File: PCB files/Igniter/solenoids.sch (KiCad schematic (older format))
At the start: 15 parts, among them Q2 N MOSFET, Q3 N MOSFET, Q4 N MOSFET, Q5 N MOSFET, Q6 N MOSFET

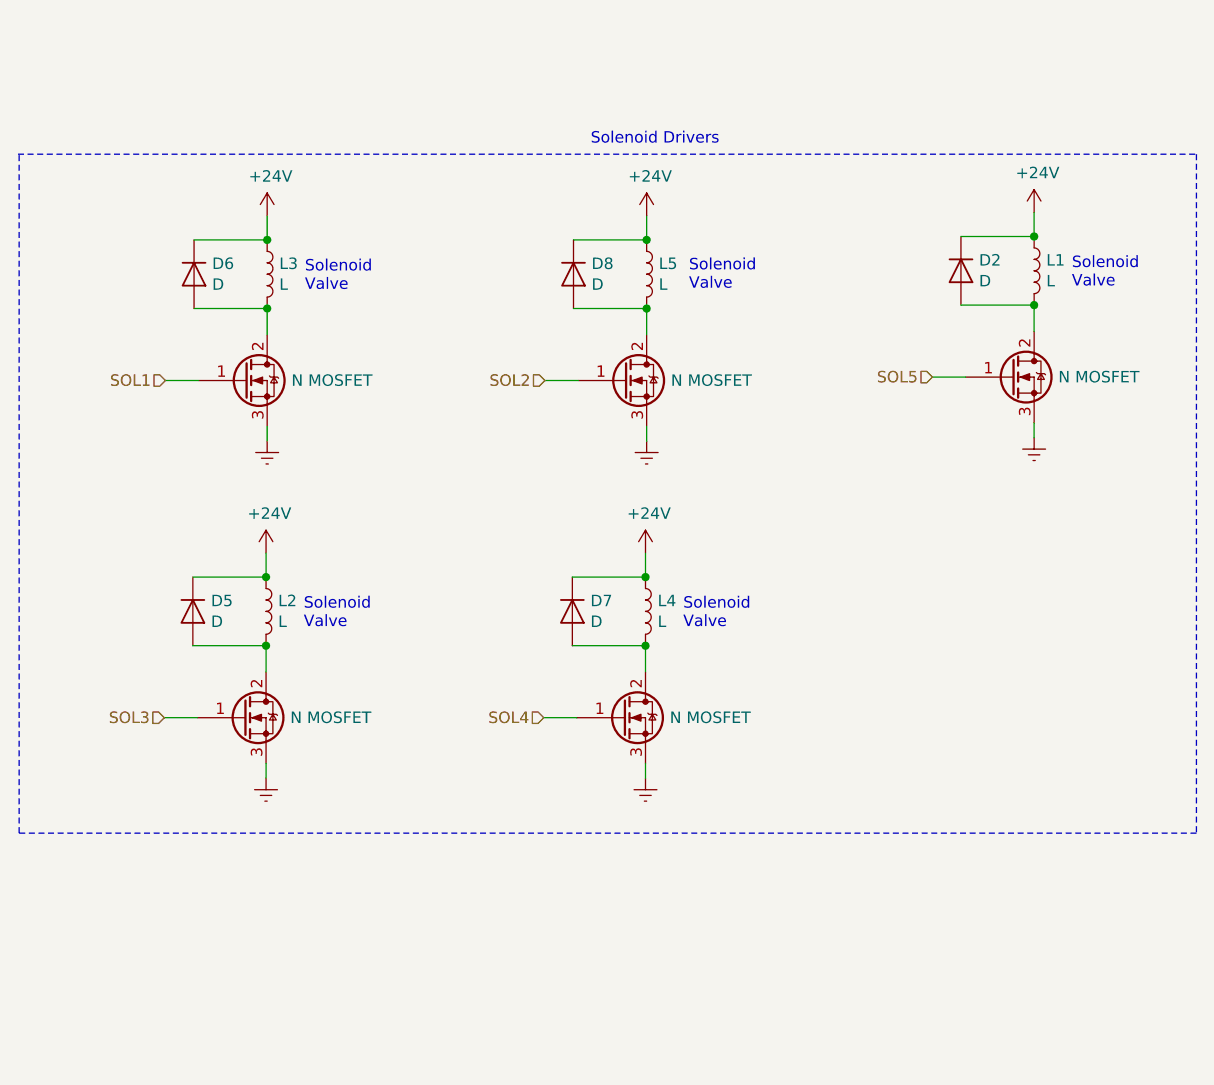
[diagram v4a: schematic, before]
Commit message: 11/1/2019
-Created bananajack footprint
-Began arranging components on board
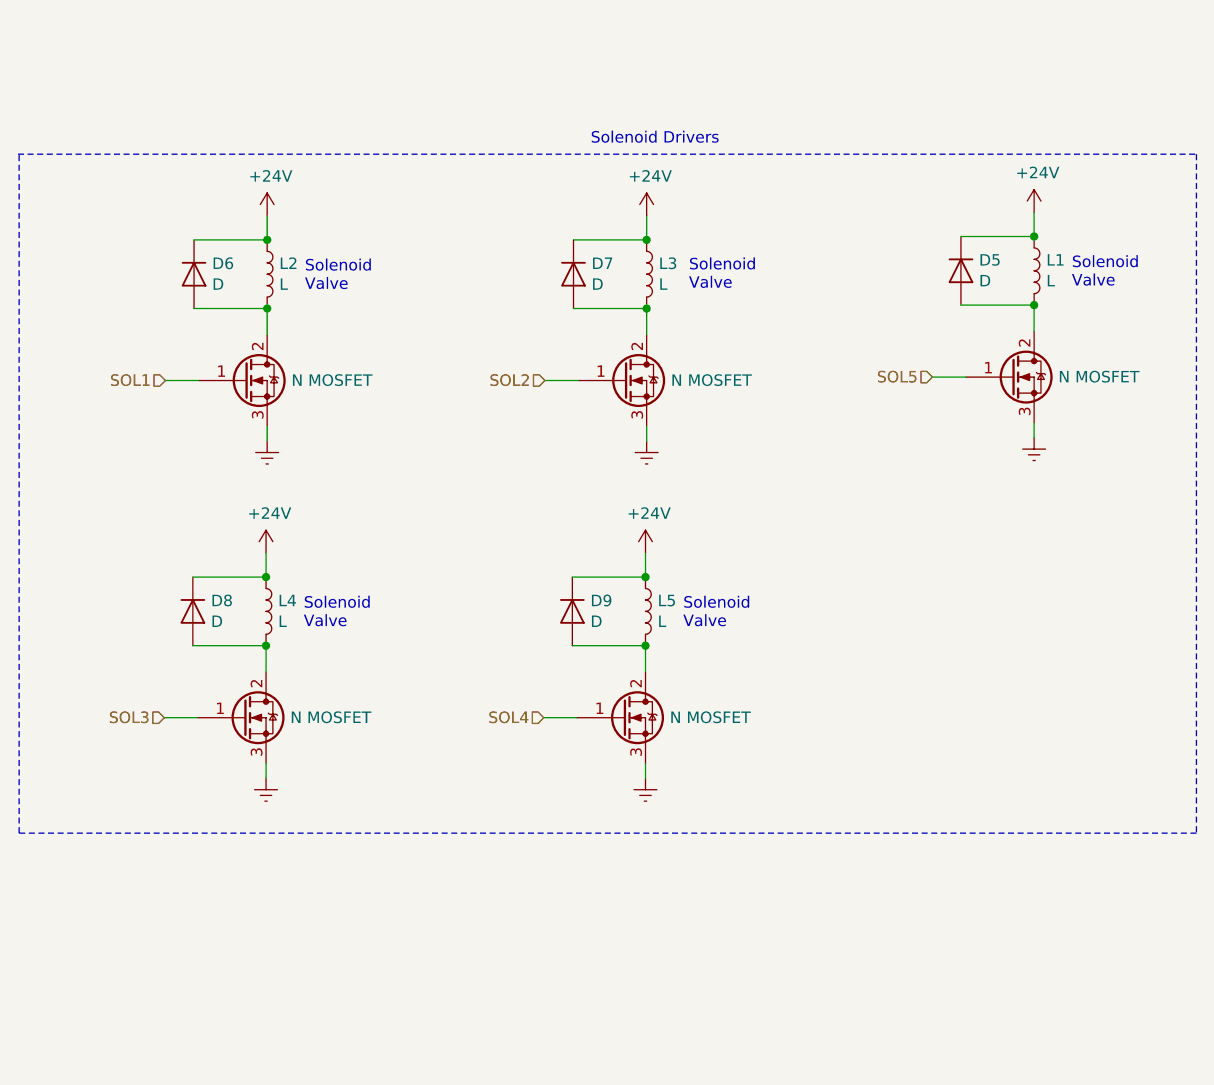
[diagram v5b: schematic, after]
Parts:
- renumbered D2 to D5, D8 to D7, D5 to D8, D7 to D9, L3 to L2, L5 to L3, L2 to L4, L4 to L5, Q4 to Q3, Q6 to Q4, Q3 to Q5, Q5 to Q6
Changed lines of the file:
@@
 LIBS:interface
 LIBS:Igniter-cache
-EELAYER 26 0
+EELAYER 29 0
 EELAYER END
 $Descr A4 11693 8268
@@
 Solenoid Drivers
 $Comp
-L Device:L L3
+L Device:L L2
 U 1 1 5DB4DF08
 P 4360 2815
-F 0 "L3" H 4413 2861 50  0000 L CNN
+F 0 "L2" H 4413 2861 50  0000 L CNN
 F 1 "L" H 4413 2770 50  0000 L CNN
 F 2 "" H 4360 2815 50  0001 C CNN
@@
 Connection ~ 4360 2965
 $Comp
-L power:GNDREF #PWR0108
+L power:GNDREF #PWR029
 U 1 1 5DB4DF2B
 P 4360 3545
-F 0 "#PWR0108" H 4360 3295 50  0001 C CNN
+F 0 "#PWR029" H 4360 3295 50  0001 C CNN
 F 1 "GNDREF" H 4365 3372 50  0001 C CNN
 F 2 "" H 4360 3545 50  0001 C CNN
@@
 	4360 3480 4360 3545
 $Comp
-L Device:L L2
+L Device:L L4
 U 1 1 5DB4DF33
 P 4355 4290
-F 0 "L2" H 4408 4336 50  0000 L CNN
+F 0 "L4" H 4408 4336 50  0000 L CNN
 F 1 "L" H 4408 4245 50  0000 L CNN
 F 2 "" H 4355 4290 50  0001 C CNN
@@
 $EndComp
 $Comp
-L Device:D D5
+L Device:D D8
 U 1 1 5DB4DF3A
 P 4035 4290
-F 0 "D5" V 3989 4369 50  0000 L CNN
+F 0 "D8" V 3989 4369 50  0000 L CNN
 F 1 "D" V 4080 4369 50  0000 L CNN
 F 2 "Diode_THT:D_DO-15_P12.70mm_Horizontal" H 4035 4290 50  0001 C CNN
@@
 Connection ~ 4355 4440
 $Comp
-L power:GNDREF #PWR0110
+L power:GNDREF #PWR033
 U 1 1 5DB4DF56
 P 4355 5020
-F 0 "#PWR0110" H 4355 4770 50  0001 C CNN
+F 0 "#PWR033" H 4355 4770 50  0001 C CNN
 F 1 "GNDREF" H 4360 4847 50  0001 C CNN
 F 2 "" H 4355 5020 50  0001 C CNN
@@
 	4355 4955 4355 5020
 $Comp
-L Device:L L5
+L Device:L L3
 U 1 1 5DB4DF5E
 P 6020 2815
-F 0 "L5" H 6073 2861 50  0000 L CNN
+F 0 "L3" H 6073 2861 50  0000 L CNN
 F 1 "L" H 6073 2770 50  0000 L CNN
 F 2 "" H 6020 2815 50  0001 C CNN
@@
 $EndComp
 $Comp
-L Device:D D8
+L Device:D D7
 U 1 1 5DB4DF65
 P 5700 2815
-F 0 "D8" V 5654 2894 50  0000 L CNN
+F 0 "D7" V 5654 2894 50  0000 L CNN
 F 1 "D" V 5745 2894 50  0000 L CNN
 F 2 "Diode_THT:D_DO-15_P12.70mm_Horizontal" H 5700 2815 50  0001 C CNN
@@
 Connection ~ 6020 2965
 $Comp
-L power:GNDREF #PWR0112
+L power:GNDREF #PWR030
 U 1 1 5DB4DF80
 P 6020 3545
-F 0 "#PWR0112" H 6020 3295 50  0001 C CNN
+F 0 "#PWR030" H 6020 3295 50  0001 C CNN
 F 1 "GNDREF" H 6025 3372 50  0001 C CNN
 F 2 "" H 6020 3545 50  0001 C CNN
@@
 	6020 3480 6020 3545
 $Comp
-L Device:L L4
+L Device:L L5
 U 1 1 5DB4DF88
 P 6015 4290
-F 0 "L4" H 6068 4336 50  0000 L CNN
+F 0 "L5" H 6068 4336 50  0000 L CNN
 F 1 "L" H 6068 4245 50  0000 L CNN
 F 2 "" H 6015 4290 50  0001 C CNN
@@
 $EndComp
 $Comp
-L Device:D D7
+L Device:D D9
 U 1 1 5DB4DF8F
 P 5695 4290
-F 0 "D7" V 5649 4369 50  0000 L CNN
+F 0 "D9" V 5649 4369 50  0000 L CNN
 F 1 "D" V 5740 4369 50  0000 L CNN
 F 2 "Diode_THT:D_DO-15_P12.70mm_Horizontal" H 5695 4290 50  0001 C CNN
@@
 Connection ~ 6015 4440
 $Comp
-L power:GNDREF #PWR0114
+L power:GNDREF #PWR034
 U 1 1 5DB4DFAB
 P 6015 5020
-F 0 "#PWR0114" H 6015 4770 50  0001 C CNN
+F 0 "#PWR034" H 6015 4770 50  0001 C CNN
 F 1 "GNDREF" H 6020 4847 50  0001 C CNN
 F 2 "" H 6015 5020 50  0001 C CNN
@@
 AR Path="/5D9BEB88/5DB4DFB4" Ref="Q?"  Part="1"
 AR Path="/5DB4DFB4" Ref="Q?"  Part="1"
-AR Path="/5DB4D508/5DB4DFB4" Ref="Q4"  Part="1"
-F 0 "Q4" H 4466 3326 50  0001 L CNN
+AR Path="/5DB4D508/5DB4DFB4" Ref="Q3"  Part="1"
+F 0 "Q3" H 4466 3326 50  0001 L CNN
 F 1 "N MOSFET" H 4466 3280 50  0000 L CNN
 F 2 "Package_TO_SOT_THT:TO-220-3_Horizontal_TabDown" H 4460 3380 50  0001 C CNN
@@
 AR Path="/5D9BEB88/5DB4DFBA" Ref="Q?"  Part="1"
 AR Path="/5DB4DFBA" Ref="Q?"  Part="1"
-AR Path="/5DB4D508/5DB4DFBA" Ref="Q6"  Part="1"
-F 0 "Q6" H 6126 3326 50  0001 L CNN
+AR Path="/5DB4D508/5DB4DFBA" Ref="Q4"  Part="1"
+F 0 "Q4" H 6126 3326 50  0001 L CNN
 F 1 "N MOSFET" H 6126 3280 50  0000 L CNN
 F 2 "Package_TO_SOT_THT:TO-220-3_Horizontal_TabDown" H 6120 3380 50  0001 C CNN
@@
 AR Path="/5D9BEB88/5DB4DFC0" Ref="Q?"  Part="1"
 AR Path="/5DB4DFC0" Ref="Q?"  Part="1"
-AR Path="/5DB4D508/5DB4DFC0" Ref="Q5"  Part="1"
-F 0 "Q5" H 6121 4801 50  0001 L CNN
+AR Path="/5DB4D508/5DB4DFC0" Ref="Q6"  Part="1"
+F 0 "Q6" H 6121 4801 50  0001 L CNN
 F 1 "N MOSFET" H 6121 4755 50  0000 L CNN
 F 2 "Package_TO_SOT_THT:TO-220-3_Horizontal_TabDown" H 6115 4855 50  0001 C CNN
@@
 AR Path="/5D9BEB88/5DB4DFC6" Ref="Q?"  Part="1"
 AR Path="/5DB4DFC6" Ref="Q?"  Part="1"
-AR Path="/5DB4D508/5DB4DFC6" Ref="Q3"  Part="1"
-F 0 "Q3" H 4461 4801 50  0001 L CNN
+AR Path="/5DB4D508/5DB4DFC6" Ref="Q5"  Part="1"
+F 0 "Q5" H 4461 4801 50  0001 L CNN
 F 1 "N MOSFET" H 4461 4755 50  0000 L CNN
 F 2 "Package_TO_SOT_THT:TO-220-3_Horizontal_TabDown" H 4455 4855 50  0001 C CNN
@@
 $EndComp
 $Comp
-L Device:D D2
+L Device:D D5
 U 1 1 5DB4DFD3
 P 7395 2800
-F 0 "D2" V 7349 2879 50  0000 L CNN
+F 0 "D5" V 7349 2879 50  0000 L CNN
 F 1 "D" V 7440 2879 50  0000 L CNN
 F 2 "Diode_THT:D_DO-15_P10.16mm_Horizontal" H 7395 2800 50  0001 C CNN
@@
 Connection ~ 7715 2950
 $Comp
-L power:GNDREF #PWR0116
+L power:GNDREF #PWR028
 U 1 1 5DB4DFEF
 P 7715 3530
-F 0 "#PWR0116" H 7715 3280 50  0001 C CNN
+F 0 "#PWR028" H 7715 3280 50  0001 C CNN
 F 1 "GNDREF" H 7720 3357 50  0001 C CNN
 F 2 "" H 7715 3530 50  0001 C CNN
@@
 SOL5
 $Comp
-L power:+24V #PWR0115
+L power:+24V #PWR026
 U 1 1 5DBB6885
 P 4360 2560
-F 0 "#PWR0115" H 4360 2410 50  0001 C CNN
+F 0 "#PWR026" H 4360 2410 50  0001 C CNN
 F 1 "+24V" H 4375 2733 50  0000 C CNN
 F 2 "" H 4360 2560 50  0001 C CNN
@@
 $EndComp
 $Comp
-L power:+24V #PWR0118
+L power:+24V #PWR027
 U 1 1 5DBB6A3C
 P 6020 2560
-F 0 "#PWR0118" H 6020 2410 50  0001 C CNN
+F 0 "#PWR027" H 6020 2410 50  0001 C CNN
 F 1 "+24V" H 6035 2733 50  0000 C CNN
 F 2 "" H 6020 2560 50  0001 C CNN
@@
 $EndComp
 $Comp
-L power:+24V #PWR0119
+L power:+24V #PWR025
 U 1 1 5DBB6B6A
 P 7715 2545
-F 0 "#PWR0119" H 7715 2395 50  0001 C CNN
+F 0 "#PWR025" H 7715 2395 50  0001 C CNN
 F 1 "+24V" H 7730 2718 50  0000 C CNN
 F 2 "" H 7715 2545 50  0001 C CNN
@@
 $EndComp
 $Comp
-L power:+24V #PWR0120
+L power:+24V #PWR031
 U 1 1 5DBB6F27
 P 4355 4035
-F 0 "#PWR0120" H 4355 3885 50  0001 C CNN
+F 0 "#PWR031" H 4355 3885 50  0001 C CNN
 F 1 "+24V" H 4370 4208 50  0000 C CNN
 F 2 "" H 4355 4035 50  0001 C CNN
@@
 $EndComp
 $Comp
-L power:+24V #PWR0121
+L power:+24V #PWR032
 U 1 1 5DBB7018
 P 6015 4035
-F 0 "#PWR0121" H 6015 3885 50  0001 C CNN
+F 0 "#PWR032" H 6015 3885 50  0001 C CNN
 F 1 "+24V" H 6030 4208 50  0000 C CNN
 F 2 "" H 6015 4035 50  0001 C CNN

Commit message: 11/2/2019
-Added board corner standoffs
-More footprint changes
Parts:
- Q2, Q3, Q4, Q5, Q6: footprint Package_TO_SOT_THT:TO-220-3_Horizontal_TabDown -> Package_TO_SOT_SMD:TO-263-3_TabPin2
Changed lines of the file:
@@
 F 0 "Q3" H 4466 3326 50  0001 L CNN
 F 1 "N MOSFET" H 4466 3280 50  0000 L CNN
-F 2 "Package_TO_SOT_THT:TO-220-3_Horizontal_TabDown" H 4460 3380 50  0001 C CNN
+F 2 "Package_TO_SOT_SMD:TO-263-3_TabPin2" H 4460 3380 50  0001 C CNN
 F 3 "~" H 4260 3280 50  0001 C CNN
 	1    4260 3280
@@
 F 0 "Q4" H 6126 3326 50  0001 L CNN
 F 1 "N MOSFET" H 6126 3280 50  0000 L CNN
-F 2 "Package_TO_SOT_THT:TO-220-3_Horizontal_TabDown" H 6120 3380 50  0001 C CNN
+F 2 "Package_TO_SOT_SMD:TO-263-3_TabPin2" H 6120 3380 50  0001 C CNN
 F 3 "~" H 5920 3280 50  0001 C CNN
 	1    5920 3280
@@
 F 0 "Q6" H 6121 4801 50  0001 L CNN
 F 1 "N MOSFET" H 6121 4755 50  0000 L CNN
-F 2 "Package_TO_SOT_THT:TO-220-3_Horizontal_TabDown" H 6115 4855 50  0001 C CNN
+F 2 "Package_TO_SOT_SMD:TO-263-3_TabPin2" H 6115 4855 50  0001 C CNN
 F 3 "~" H 5915 4755 50  0001 C CNN
 	1    5915 4755
@@
 F 0 "Q5" H 4461 4801 50  0001 L CNN
 F 1 "N MOSFET" H 4461 4755 50  0000 L CNN
-F 2 "Package_TO_SOT_THT:TO-220-3_Horizontal_TabDown" H 4455 4855 50  0001 C CNN
+F 2 "Package_TO_SOT_SMD:TO-263-3_TabPin2" H 4455 4855 50  0001 C CNN
 F 3 "~" H 4255 4755 50  0001 C CNN
 	1    4255 4755
@@
 F 0 "Q2" H 7821 3311 50  0001 L CNN
 F 1 "N MOSFET" H 7821 3265 50  0000 L CNN
-F 2 "Package_TO_SOT_THT:TO-220-3_Horizontal_TabDown" H 7815 3365 50  0001 C CNN
+F 2 "Package_TO_SOT_SMD:TO-263-3_TabPin2" H 7815 3365 50  0001 C CNN
 F 3 "~" H 7615 3265 50  0001 C CNN
 	1    7615 3265

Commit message: 11/3/2019
-Added molex footprints for p ducer and solenoid connection
-Completed blade fuse holder footprint
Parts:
- L1, L2, L3, L4, L5: footprint (none) -> Connector_Molex:Molex_Mini-Fit_Jr_5566-04A_2x02_P4.20mm_Vertical
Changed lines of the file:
@@
 F 0 "L2" H 4413 2861 50  0000 L CNN
 F 1 "L" H 4413 2770 50  0000 L CNN
-F 2 "" H 4360 2815 50  0001 C CNN
+F 2 "Connector_Molex:Molex_Mini-Fit_Jr_5566-04A_2x02_P4.20mm_Vertical" H 4360 2815 50  0001 C CNN
 F 3 "~" H 4360 2815 50  0001 C CNN
 	1    4360 2815
@@
 F 0 "L4" H 4408 4336 50  0000 L CNN
 F 1 "L" H 4408 4245 50  0000 L CNN
-F 2 "" H 4355 4290 50  0001 C CNN
+F 2 "Connector_Molex:Molex_Mini-Fit_Jr_5566-04A_2x02_P4.20mm_Vertical" H 4355 4290 50  0001 C CNN
 F 3 "~" H 4355 4290 50  0001 C CNN
 	1    4355 4290
@@
 F 0 "L3" H 6073 2861 50  0000 L CNN
 F 1 "L" H 6073 2770 50  0000 L CNN
-F 2 "" H 6020 2815 50  0001 C CNN
+F 2 "Connector_Molex:Molex_Mini-Fit_Jr_5566-04A_2x02_P4.20mm_Vertical" H 6020 2815 50  0001 C CNN
 F 3 "~" H 6020 2815 50  0001 C CNN
 	1    6020 2815
@@
 F 0 "L5" H 6068 4336 50  0000 L CNN
 F 1 "L" H 6068 4245 50  0000 L CNN
-F 2 "" H 6015 4290 50  0001 C CNN
+F 2 "Connector_Molex:Molex_Mini-Fit_Jr_5566-04A_2x02_P4.20mm_Vertical" H 6015 4290 50  0001 C CNN
 F 3 "~" H 6015 4290 50  0001 C CNN
 	1    6015 4290
@@
 F 0 "L1" H 7768 2846 50  0000 L CNN
 F 1 "L" H 7768 2755 50  0000 L CNN
-F 2 "" H 7715 2800 50  0001 C CNN
+F 2 "Connector_Molex:Molex_Mini-Fit_Jr_5566-04A_2x02_P4.20mm_Vertical" H 7715 2800 50  0001 C CNN
 F 3 "~" H 7715 2800 50  0001 C CNN
 	1    7715 2800
